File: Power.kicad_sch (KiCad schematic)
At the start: 38 parts, among them J2 Screw_Terminal_01x03, T1 Transformer_1P_1S, T2 Transformer_SP_2S, U2 SN6507DGQ, U4 LD3985G33R_TSOT23, U6 LF50_TO252, U7 LD3985G33R_TSOT23

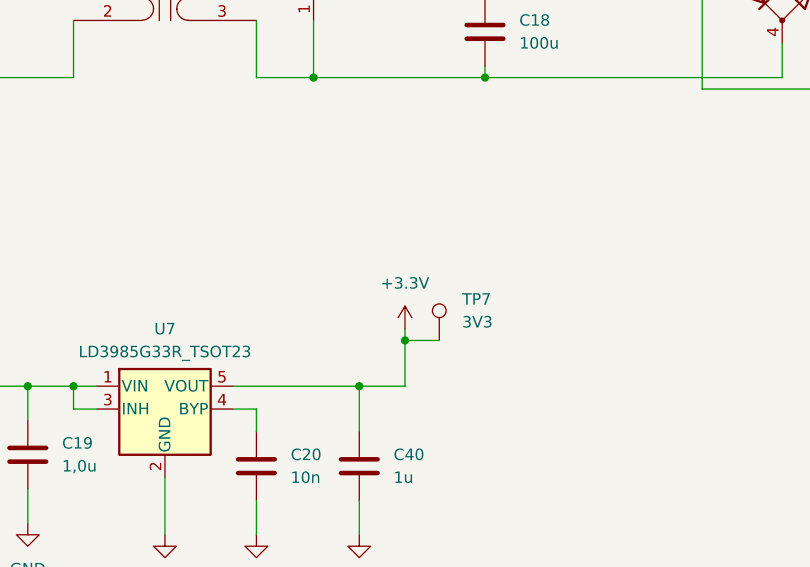
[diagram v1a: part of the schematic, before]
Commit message: I2C pullups
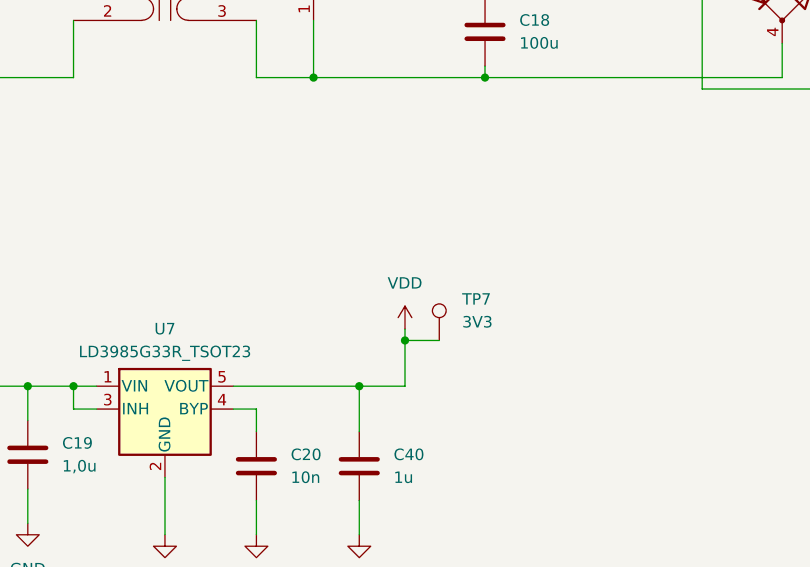
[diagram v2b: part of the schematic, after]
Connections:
- net +3.3V: no longer C40.1, TP7.1, U7.5 (VOUT)
- new net VDD: C40.1, TP7.1, U7.5 (VOUT)
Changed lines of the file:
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@@
-    )
-  )
-  (symbol (lib_id "power:+3.3V") (at 142.24 76.2 0) (unit 1)
-    (in_bom yes) (on_board yes) (dnp no) (fields_autoplaced)
-    (property "Reference" "#PWR064" (at 142.24 80.01 0)
-      (effects (font (size 1.27 1.27)) hide)
-    )
-    (property "Value" "+3.3V" (at 142.24 71.12 0)
-      (effects (font (size 1.27 1.27)))
-    )
-    (property "Footprint" "" (at 142.24 76.2 0)
-      (effects (font (size 1.27 1.27)) hide)
-    )
-    (property "Datasheet" "" (at 142.24 76.2 0)
-      (effects (font (size 1.27 1.27)) hide)
-    )
-    (pin "1")
-    (instances
-      (project "Eng_Thesis"
-        (path "/97bd1b5a-123d-47f8-a974-72569e0e2197/403da9b1-219c-43a2-869b-4f14604ce1cf"
-          (reference "#PWR064") (unit 1)
-        )
-      )
     )
   )
@@
         )
       )
+    )
+  )
+  (symbol (lib_id "power:VDD") (at 142.24 76.2 0) (unit 1)
+    (in_bom yes) (on_board yes) (dnp no) (fields_autoplaced)
+    (property "Reference" "#PWR070" (at 142.24 80.01 0)
+      (effects (font (size 1.27 1.27)) hide)
+    )
+    (property "Value" "VDD" (at 142.24 71.12 0)
+      (effects (font (size 1.27 1.27)))
+    )
+    (property "Footprint" "" (at 142.24 76.2 0)
+      (effects (font (size 1.27 1.27)) hide)
+    )
+    (property "Datasheet" "" (at 142.24 76.2 0)
+      (effects (font (size 1.27 1.27)) hide)
+    )
+    (pin "1")
+    (instances
+      (project "Eng_Thesis"
+        (path "/97bd1b5a-123d-47f8-a974-72569e0e2197/403da9b1-219c-43a2-869b-4f14604ce1cf"
+          (reference "#PWR070") (unit 1)
+        )
+      )

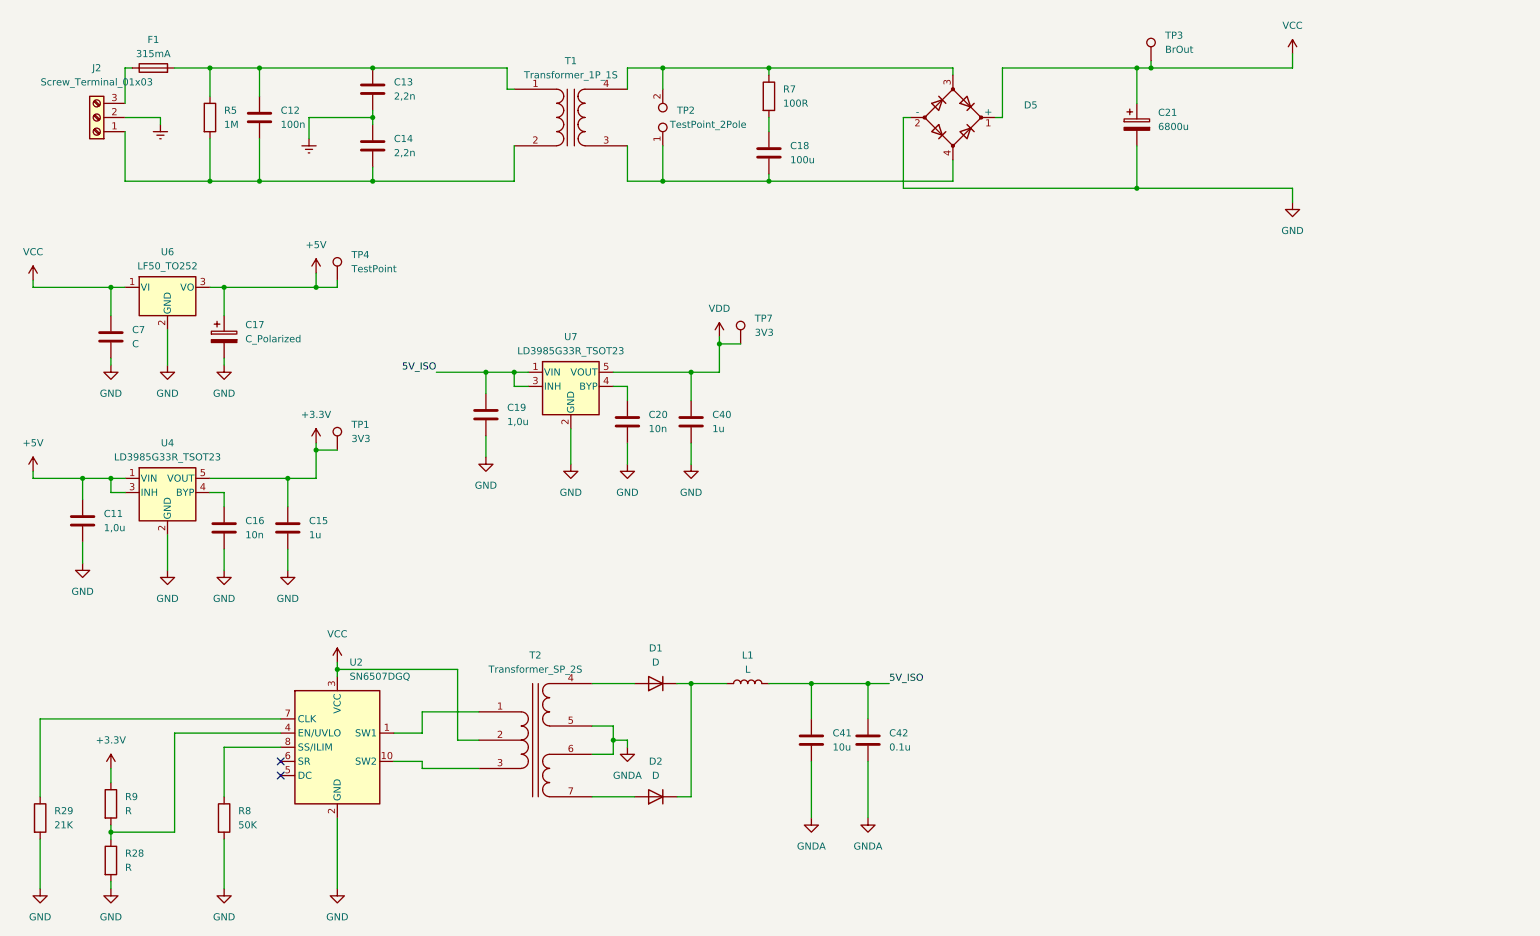
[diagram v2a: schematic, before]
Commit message: v0.1 of schematic + most of footprints/links
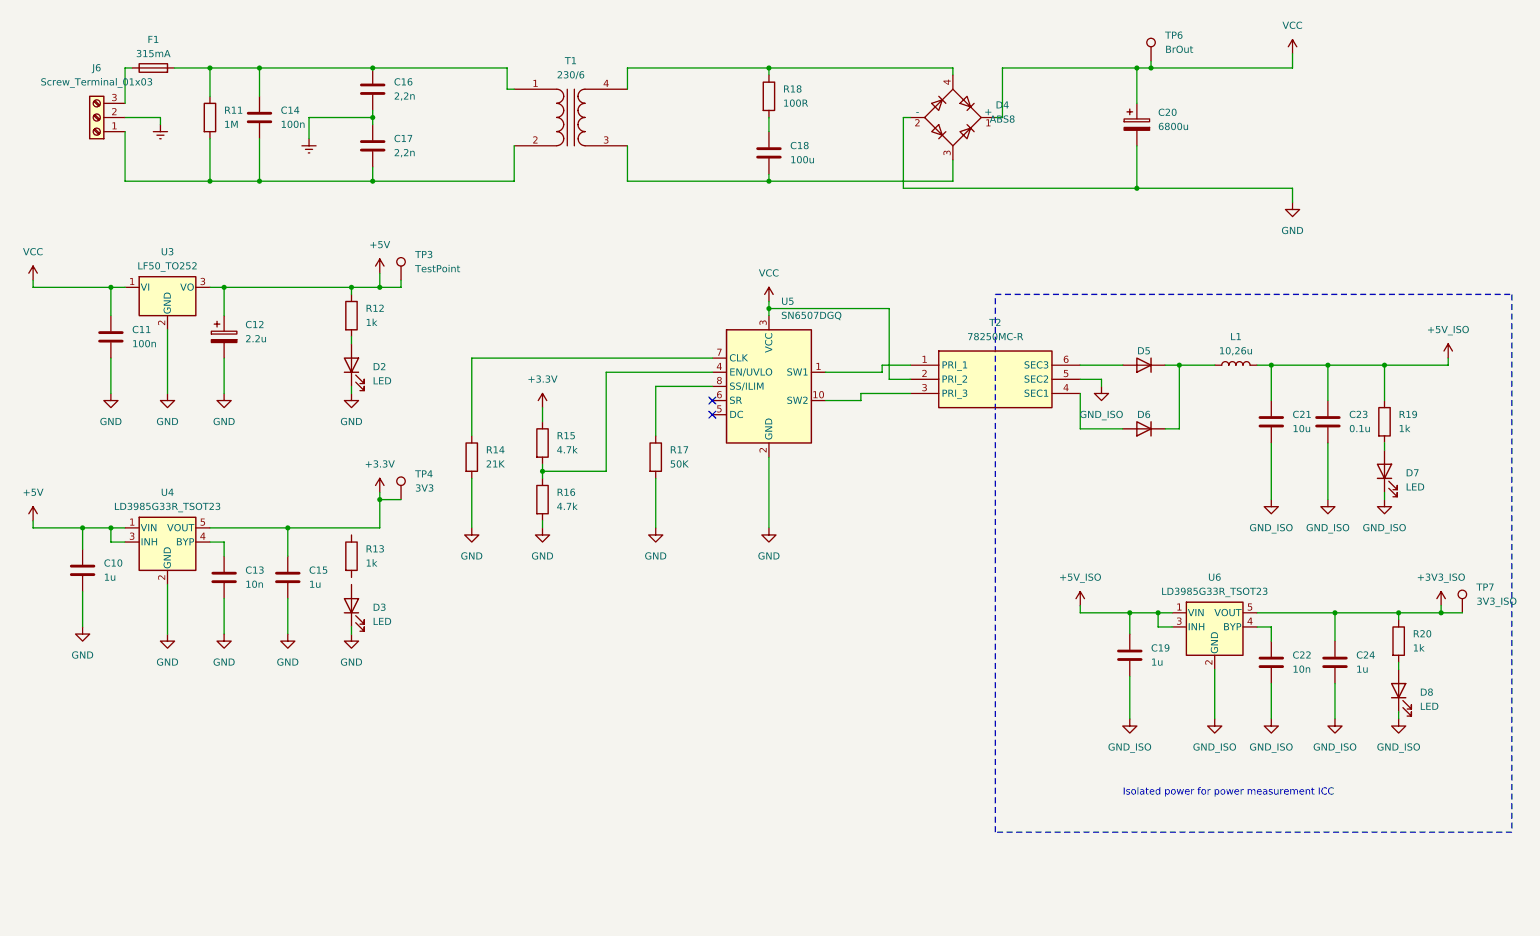
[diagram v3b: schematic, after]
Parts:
- removed C20: 10n, symbol Device:C
- removed C40: 1u, symbol Device:C
- removed C7: C, symbol Device:C
- removed D1: D, symbol Device:D
- removed D5: MB8FTR, symbol Device:D_Bridge_+-AA
- removed T2: Transformer_SP_2S, symbol Device:Transformer_SP_2S
- removed TP2: TestPoint_2Pole, symbol Connector:TestPoint_2Pole
- added C11: 100n, Capacitor_SMD:C_0201_0603Metric_Pad0.64x0.40mm_HandSolder, symbol Device:C
- added C22: 10n, Capacitor_SMD:C_0603_1608Metric_Pad1.08x0.95mm_HandSolder, symbol Device:C
- added C24: 1u, Capacitor_SMD:C_0603_1608Metric_Pad1.08x0.95mm_HandSolder, symbol Device:C
- added D2, D3, D7, D8: LED, LED_SMD:LED_0603_1608Metric_Pad1.05x0.95mm_HandSolder, symbol Device:LED
- added D4: ABS8, Diode_SMD:Diode_Bridge_Diotec_ABS, symbol Diode_Bridge:ABS8
- added D5: BAT165E6327HTSA1, Diode_SMD:D_SOD-323F, symbol Device:D
- added R12, R13, R19, R20: 1k, symbol Device:R
- added T2: 78250MC-R, LibLoader:SOP254P1270X660-6N, symbol LibLoader:78250MC-R
- C10: renamed from C11; value 1,0u -> 1u; footprint (none) -> Capacitor_SMD:C_0603_1608Metric_Pad1.08x0.95mm_HandSolder
- C12: renamed from C17; value C_Polarized -> 2.2u; footprint (none) -> Capacitor_SMD:CP_Elec_4x5.3
- C13: renamed from C16; footprint (none) -> Capacitor_SMD:C_0603_1608Metric_Pad1.08x0.95mm_HandSolder
- C14: renamed from C12; footprint (none) -> Capacitor_THT:C_Rect_L18.0mm_W6.0mm_P15.00mm_FKS3_FKP3
- C15: footprint (none) -> Capacitor_SMD:C_0603_1608Metric_Pad1.08x0.95mm_HandSolder
- C16: renamed from C13; footprint (none) -> Capacitor_THT:C_Disc_D10.5mm_W5.0mm_P7.50mm
- C17: renamed from C14; footprint (none) -> Capacitor_THT:C_Disc_D10.5mm_W5.0mm_P7.50mm
- C19: value 1,0u -> 1u; footprint (none) -> Capacitor_SMD:C_0603_1608Metric_Pad1.08x0.95mm_HandSolder
- C20: renamed from C21; footprint (none) -> Capacitor_THT:CP_Radial_D18.0mm_P7.50mm
- C21: renamed from C41; footprint (none) -> Capacitor_SMD:C_0603_1608Metric_Pad1.08x0.95mm_HandSolder
- C23: renamed from C42; footprint (none) -> Capacitor_SMD:C_0201_0603Metric_Pad0.64x0.40mm_HandSolder
- D6: renamed from D2; value D -> BAT165E6327HTSA1; footprint (none) -> Diode_SMD:D_SOD-323F
- F1: footprint (none) -> Fuse:Fuse_2920_7451Metric_Pad2.10x5.45mm_HandSolder
- L1: value L -> 10,26u; footprint (none) -> Inductor_SMD:L_1210_3225Metric_Pad1.42x2.65mm_HandSolder
- R15: renamed from R9; value R -> 4.7k
- R16: renamed from R28; value R -> 4.7k
- T1: value Transformer_1P_1S -> 230/6; footprint (none) -> Transformer_THT:TSZZ4.5003M
- TP3: renamed from TP4; footprint (none) -> TestPoint:TestPoint_Pad_1.5x1.5mm
- TP4: renamed from TP1; footprint (none) -> TestPoint:TestPoint_Pad_1.5x1.5mm
- TP6: renamed from TP3; footprint (none) -> TestPoint:TestPoint_Pad_1.5x1.5mm
- TP7: value 3V3 -> 3V3_ISO; footprint (none) -> TestPoint:TestPoint_Pad_1.5x1.5mm
- renumbered J2 to J6, R5 to R11, R29 to R14, R8 to R17, R7 to R18, U6 to U3, U2 to U5, U7 to U6
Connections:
- net +5V: now also R12.1
- net GND: now also C11.2, D2.1 (K), D3.1 (K), D4.2 (-); no longer C19.2, U6.2 (GND)
- net VCC: now also C11.1, D4.1 (+), T2.2 (PRI_2)
- net at U5.1 (SW1): now also T2.1 (PRI_1)
- net at U5.10 (SW2): now also T2.3 (PRI_3)
- net at D6.2 (A): now also T2.4 (SEC1)
- net at D6.1 (K), L1.1: now also D5.1 (K)
- net at C18.2, T1.3 (SA): now also D4.3
- net at R18.1, T1.4 (SB): now also D4.4
- net at U6.4 (BYP): now also C22.1
- net 5V_ISO renamed +5V_ISO
- net +5V_ISO: now also R19.1
- net GNDA renamed GND_ISO
- net GND_ISO: now also C19.2, U6.2 (GND), C22.2, C24.2, D7.1 (K), D8.1 (K), T2.5 (SEC2)
- net VDD renamed +3V3_ISO
- net +3V3_ISO: now also C24.1, R20.1
- new net: D2.2 (A), R12.2
- new net: D7.2 (A), R19.2
- new net: D8.2 (A), R20.2
- new net: D5.2 (A), T2.6 (SEC3)
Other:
- note added: "Isolated power for power measurement ICC"
- moved on the sheet: C10, C13, C21, C23, D6, L1, R14, R15, R16, R17, TP3, TP4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
